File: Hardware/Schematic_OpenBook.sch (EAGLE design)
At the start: 103 parts, among them IC1 XC6220A331MR-G, IC4 XC6220A331MR-G, J1 FH34SRJ-24S-0.5SH_99_, J2 SAMACSYS_PARTS_USB4110-GF-A, J3 QWIIC_RIGHT_ANGLE, J4 112A-TAAR-R03_ATTEND, Q1 20V/4.2A/52mΩ/1.4W, Q2 20V/4.2A/52mΩ/1.4W, Q3 SI1308EDL-T1-GE3, U1 W25Q512JVEIQ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

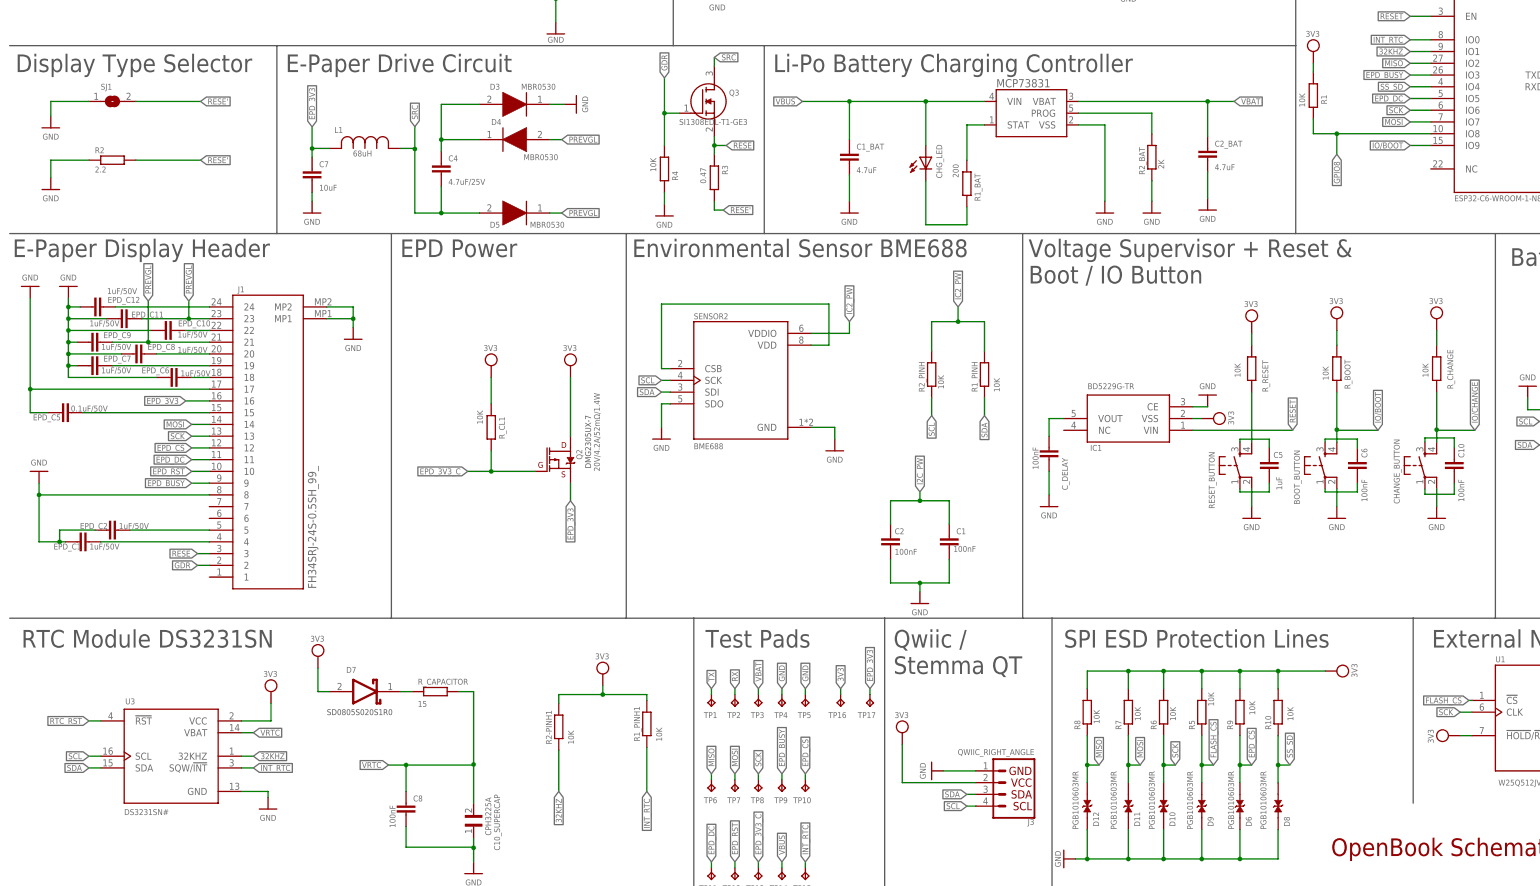
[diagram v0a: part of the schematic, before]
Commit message: Update schematic, reversing component pins
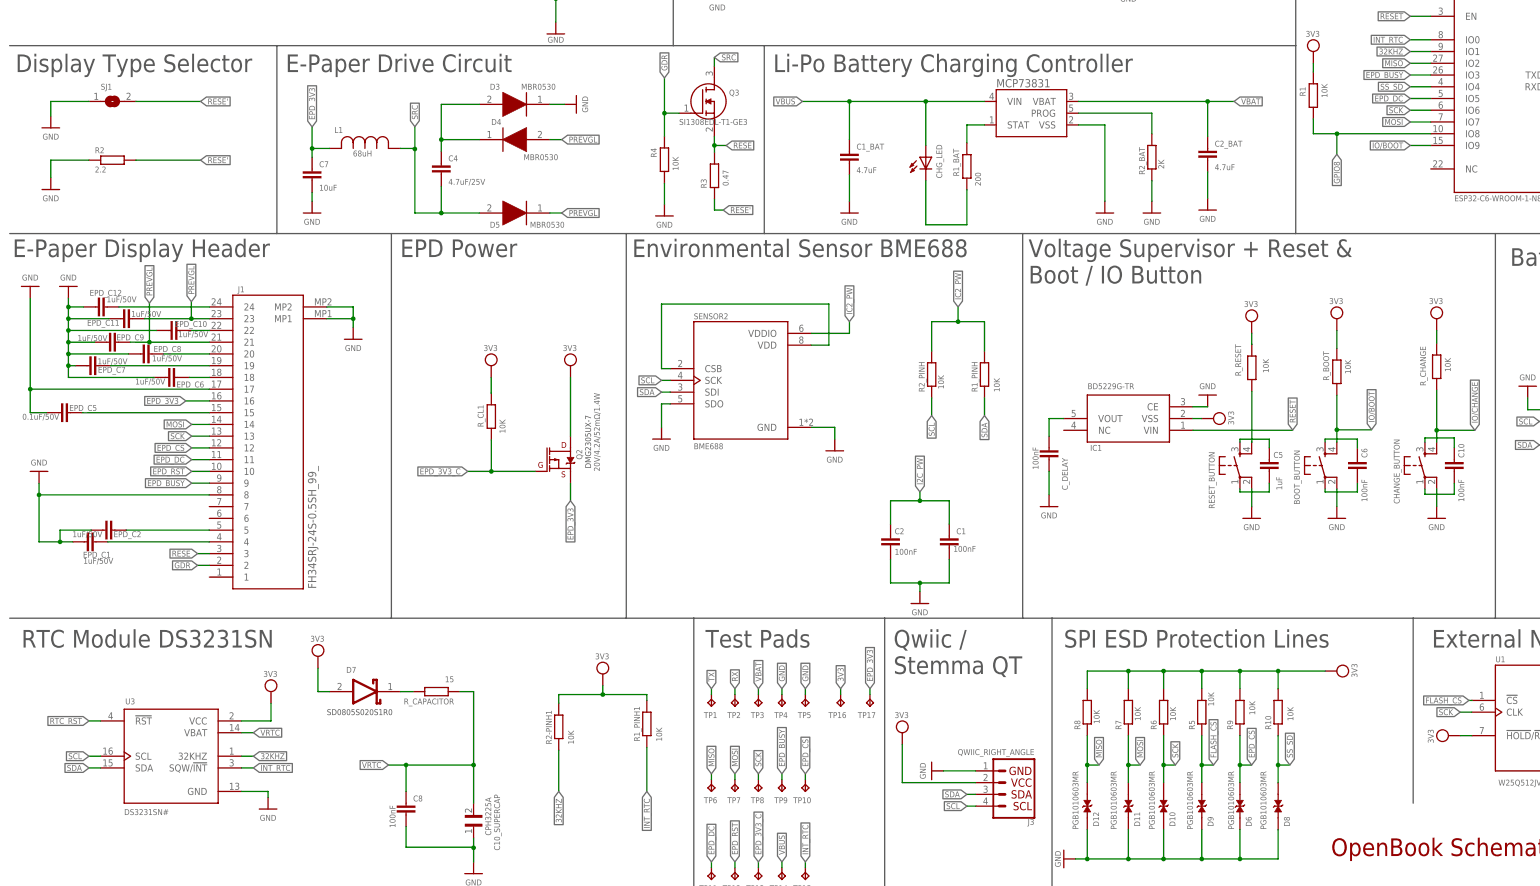
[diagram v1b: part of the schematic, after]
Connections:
- removed net N$22: EPD_C2.2, J1.5
- new net N$17: EPD_C1.1, J1.4
- net 3V3: now also R1.1, R_BOOT.1, R_CHANGE.1, R_CL1.1, R_RESET.1; no longer R1.2, R_BOOT.2, R_CHANGE.2, R_CL1.2, R_RESET.2
- net EPD_3V3_C: now also R_CL1.2; no longer R_CL1.1
- net GDR: now also R4.1; no longer R4.2
- net GND: now also EPD_C1.2, EPD_C10.2, EPD_C11.2, EPD_C12.2, EPD_C2.2, EPD_C5.2, EPD_C6.2, EPD_C7.2, EPD_C8.2, EPD_C9.2, R4.2; no longer EPD_C1.1, EPD_C10.1, EPD_C11.1, EPD_C12.1, EPD_C2.1, EPD_C5.1, EPD_C6.1, EPD_C7.1, EPD_C8.1, EPD_C9.1, R4.1
- net GPIO8: now also R1.2; no longer R1.1
- net IO/BOOT: now also R_BOOT.2; no longer R_BOOT.1
- net IO/CHANGE: now also R_CHANGE.2; no longer R_CHANGE.1
- net N$10: now also R1_BAT.1; no longer R1_BAT.2
- net N$11: now also R1_BAT.2; no longer R1_BAT.1
- net N$13: now also EPD_C10.1; no longer EPD_C10.2
- net N$14: now also R_CAPACITOR.2; no longer R_CAPACITOR.1
- net N$15: now also EPD_C8.1; no longer EPD_C8.2
- net N$16: now also EPD_C7.1; no longer EPD_C7.2
- net N$18: now also R_RESET.2; no longer R_RESET.1
- net N$19: now also EPD_C6.1; no longer EPD_C6.2
- net N$20: now also EPD_C2.1, J1.5; no longer EPD_C1.2, J1.4
- net N$21: now also EPD_C5.1; no longer EPD_C5.2
- net N$9: now also EPD_C12.1; no longer EPD_C12.2
- net PREVGL: now also EPD_C11.1, EPD_C9.1; no longer EPD_C11.2, EPD_C9.2
- net RESE: now also R3.1; no longer R3.2
- net RESE': now also R3.2; no longer R3.1
- net VRTC: now also R_CAPACITOR.1; no longer R_CAPACITOR.2
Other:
- moved on the sheet: EPD_C1, EPD_C10, EPD_C11, EPD_C12, EPD_C2, EPD_C5, EPD_C6, EPD_C7, EPD_C8, EPD_C9, R1, R1_BAT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
